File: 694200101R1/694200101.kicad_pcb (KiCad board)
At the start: 2 copper layers, 438.6 x 125.8 mm, 393 parts, among them J1 USB4085-GF-A, J2 Conn_01x05_Male, J3 Conn_01x02_Male, SW1 MX_SW, SW10 MX_SW, SW100 MX_SW, SW101 MX_SW, SW102 MX_SW, SW103 MX_SW, SW104 MX_SW, SW105 MX_SW, SW106 MX_SW, SW107 MX_SW, SW11 MX_SW, SW12 MX_SW, SW13 MX_SW, SW14 MX_SW, SW15 MX_SW, SW16 MX_SW, SW17 MX_SW, SW18 MX_SW, SW19 MX_SW, SW2 MX_SW, SW20 MX_SW, SW21 MX_SW, SW22 MX_SW, SW23 MX_SW, SW24 MX_SW, SW25 MX_SW, SW26 MX_SW, SW27 MX_SW, SW28 MX_SW, SW29 MX_SW, SW3 MX_SW, SW30 MX_SW, SW31 MX_SW, SW32 MX_SW, SW33 MX_SW, SW34 MX_SW, SW35 MX_SW, SW36 MX_SW, SW37 MX_SW, SW38 MX_SW, SW39 MX_SW, SW4 MX_SW, SW40 MX_SW, SW41 MX_SW, SW42 MX_SW, SW43 MX_SW, SW44 MX_SW, SW45 MX_SW, SW46 MX_SW, SW47 MX_SW, SW48 MX_SW, SW49 MX_SW, SW5 MX_SW, SW50 MX_SW, SW51 MX_SW, SW52 MX_SW, SW53 MX_SW, SW54 MX_SW, SW55 MX_SW, SW56 MX_SW, SW57 MX_SW, SW58 MX_SW, SW59 MX_SW, SW6 MX_SW, SW60 MX_SW, SW61 MX_SW, SW62 MX_SW, SW63 MX_SW, SW64 MX_SW, SW65 MX_SW, SW66 MX_SW, SW67 MX_SW, SW68 MX_SW, SW69 MX_SW, SW7 MX_SW, SW70 MX_SW, SW71 MX_SW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

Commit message: Updated PCB Footprints
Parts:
- CR1: value SMAJ9.0CA -> SMASeries_LTF
- F1: value 1210L150THWR -> 1210LSeries_LTF
- U1: value AP2114HA-3.3TRG1 -> SOT-223_DIO
- U5, U6: value IS31FL3733B-QFLS4-TR -> QFN-48_ISI

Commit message: row 6 row traces
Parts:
- CR1: value SMASeries_LTF -> SMAJ9.0CA
- F1: value 1210LSeries_LTF -> 1210L150THWR
- U1: value SOT-223_DIO -> AP2114HA-3.3TRG1
- U5, U6: value QFN-48_ISI -> IS31FL3733B-QFLS4-TR
- moved D96 0.35 mm to (389.9, 46.5)
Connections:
- SW106 pad 1: Net-(D107-Pad2) -> COL_22
- SW106 pad 2: COL_22 -> Net-(D107-Pad2)
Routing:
- net ROW_6: track 0.00 -> 414.6 mm
- net Net-(D94-Pad2): track 0.00 -> 6.35 mm
- net Net-(D99-Pad2): track 0.00 -> 5.18 mm
- net Net-(D19-Pad2): track 0.00 -> 4.81 mm
- net Net-(D78-Pad2): track 0.00 -> 4.80 mm
- net Net-(D68-Pad2): track 0.00 -> 4.71 mm
- net Net-(D93-Pad2): track 0.00 -> 4.67 mm
- net Net-(D54-Pad2): track 0.00 -> 4.58 mm
- net Net-(D67-Pad2): track 0.00 -> 4.57 mm
- net Net-(D5-Pad2): track 0.00 -> 4.54 mm
- net Net-(D108-Pad2): track 0.00 -> 4.38 mm
- net Net-(D8-Pad2): track 0.00 -> 4.37 mm
- net Net-(D70-Pad2): track 0.00 -> 4.31 mm
- net Net-(D37-Pad2): track 0.00 -> 4.24 mm
- net Net-(D73-Pad2): track 0.00 -> 4.22 mm
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
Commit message: Added Mounting Holes and alignment slots
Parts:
- added H1: PCB Mounting Hole, MountingHole:MountingHole_3.5mm, F.Cu at (395.0, 130.8)
- added H2: PCB Common Earth, MountingHole:MountingHole_3.5mm_Pad_TopBottom, F.Cu at (209.6, -6.35)
- added H3: PCB Mounting Hole, MountingHole:MountingHole_3.5mm, F.Cu at (195.6, 134.6)
- added H4: PCB Mounting Hole, MountingHole:MountingHole_3.5mm, F.Cu at (27.9, 132.1)
- added H5: PCB Mounting Hole, MountingHole:MountingHole_3.5mm, F.Cu at (416.6, -5.08)
- added H6: PCB Mounting Hole, MountingHole:MountingHole_3.5mm, F.Cu at (33.0, -6.35)
- added H7: Mounting Slot, keyboard_parts:MountingHole_M2_edge, F.Cu at (436.9, 85.1)
- added H8: Mounting Slot, keyboard_parts:MountingHole_M2_edge, F.Cu at (1.27, 83.8)

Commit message: switch row 3
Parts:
- moved H2 222.9 mm to (432.1, 6.35)
- moved H1 38.8 mm to (432.1, 119.4)
- moved H6 29.5 mm to (6.35, 6.35)
- moved H4 25.0 mm to (6.35, 119.4)
- moved H5 5.48 mm to (411.2, -6.35)
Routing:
- net ROW_5: track 0.00 -> 392.4 mm
- net ROW_4: track 0.00 -> 300.9 mm
- net ROW_3: track 0.00 -> 292.9 mm
- net Net-(D69-Pad2): track 0.00 -> 3.82 mm

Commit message: side slots and switch row 2
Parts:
- moved H2 138.8 mm to (293.2, 6.35)
- moved H8 1.42 mm to (1.91, 85.1)
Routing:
- net ROW_2: track 0.00 -> 414.8 mm, vias 0 -> 2
- net ROW_3: track 292.9 -> 399.3 mm
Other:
- rule trace_min: 0.2 -> 0.2032
- rule via_min_drill: 0.3 -> 0.2032
- rule via_min_size: 0.4 -> 0.3048
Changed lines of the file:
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@@
     (thickness 1.6)
     (drawings 2085)
-    (tracks 790)
+    (tracks 817)
     (zones 0)
     (modules 401)
@@
     (user_trace_width 1.016)
     (user_trace_width 2.032)
+    (user_trace_width 2.54)
     (trace_clearance 0.0254)
     (zone_clearance 0.127)
     (zone_45_only yes)
-    (trace_min 0.2)
+    (trace_min 0.2032)
     (via_size 0.5588)
     (via_drill 0.3048)
-    (via_min_size 0.4)
-    (via_min_drill 0.3)
+    (via_min_size 0.3048)
+    (via_min_drill 0.2032)
     (user_via 0.381 0.2032)
     (user_via 0.508 0.254)
@@
     (uvia_dia 0.3)
     (uvia_drill 0.1)
+    (diff_pair_width 0.2032)
+    (diff_pair_gap 0.25)
     (add_net +3V3)
     (add_net +5V)
@@
   )
   (module keyboard_parts:MountingHole_M2_edge (layer F.Cu)
-    (at 1.27 83.82)
+    (at 1.905 85.09)
     (descr "Mounting Hole 4mm, no annular")
     (tags "mounting hole 4mm no annular")
@@
   )
   (module MountingHole:MountingHole_3.5mm_Pad_TopBottom (layer F.Cu)
-    (at 432.054 6.35)
+    (at 293.243 6.35)
     (descr "Mounting Hole 3.5mm")
     (tags "mounting hole 3.5mm")
@@
   (segment (start 18.335 44.385) (end 18.5 44.55) (width 0.254) (layer B.Cu) (net 7))
   (segment (start 18.335 40.64) (end 18.335 44.385) (width 0.254) (layer B.Cu) (net 7))
+  (segment (start 18.5 48.449999) (end 94.169999 48.449999) (width 0.254) (layer B.Cu) (net 8))
+  (segment (start 94.5 48.449999) (end 170.75 48.449999) (width 0.254) (layer B.Cu) (net 8))
+  (segment (start 170.75 48.449999) (end 208.75 48.449999) (width 0.254) (layer B.Cu) (net 8))
+  (segment (start 208.75 48.449999) (end 247.0375 48.449999) (width 0.254) (layer B.Cu) (net 8))
+  (segment (start 247.0375 48.449999) (end 253.046999 48.449999) (width 0.254) (layer B.Cu) (net 8))
+  (segment (start 253.046999 48.449999) (end 254.381 49.784) (width 0.254) (layer B.Cu) (net 8))
+  (segment (start 304.864001 48.449999) (end 308.75 48.449999) (width 0.254) (layer B.Cu) (net 8))
+  (segment (start 303.53 49.784) (end 304.864001 48.449999) (width 0.254) (layer B.Cu) (net 8))
+  (segment (start 275.75 49.624) (end 275.59 49.784) (width 0.254) (layer B.Cu) (net 8))
+  (segment (start 275.75 48.449999) (end 275.75 49.624) (width 0.254) (layer B.Cu) (net 8))
+  (segment (start 275.59 49.784) (end 303.53 49.784) (width 0.254) (layer B.Cu) (net 8))
+  (segment (start 254.381 49.784) (end 275.59 49.784) (width 0.254) (layer B.Cu) (net 8))
+  (segment (start 308.75 48.449999) (end 328 48.449999) (width 0.254) (layer B.Cu) (net 8))
+  (segment (start 347.0375 48.449999) (end 349.949001 48.449999) (width 0.254) (layer B.Cu) (net 8))
+  (segment (start 428.25 48.449999) (end 408.9625 48.449999) (width 0.254) (layer B.Cu) (net 8))
+  (segment (start 328 48.449999) (end 333.437999 48.449999) (width 0.254) (layer B.Cu) (net 8))
+  (segment (start 333.437999 48.449999) (end 339.406999 48.449999) (width 0.254) (layer B.Cu) (net 8))
+  (segment (start 339.406999 48.449999) (end 339.406999 48.449999) (width 0.254) (layer B.Cu) (net 8))
+  (via (at 339.406999 48.449999) (size 0.508) (drill 0.254) (layers F.Cu B.Cu) (net 8))
+  (segment (start 349.949001 48.449999) (end 408.9625 48.449999) (width 0.254) (layer B.Cu) (net 8))
+  (via (at 349.949001 48.449999) (size 0.508) (drill 0.254) (layers F.Cu B.Cu) (net 8))
+  (segment (start 339.406999 48.449999) (end 349.949001 48.449999) (width 0.254) (layer F.Cu) (net 8))
   (segment (start 23.0975 63.1475) (end 23.25 63.3) (width 0.254) (layer B.Cu) (net 9))
   (segment (start 23.0975 59.69) (end 23.0975 63.1475) (width 0.254) (layer B.Cu) (net 9))
@@
   (segment (start 263.271 65.405) (end 286.385 65.405) (width 0.254) (layer B.Cu) (net 10))
   (segment (start 252.476 65.405) (end 263.271 65.405) (width 0.254) (layer B.Cu) (net 10))
+  (segment (start 309 67.199999) (end 328 67.199999) (width 0.254) (layer B.Cu) (net 10))
+  (segment (start 328 67.199999) (end 370.75 67.199999) (width 0.254) (layer B.Cu) (net 10))
+  (segment (start 370.75 67.199999) (end 408.75 67.199999) (width 0.254) (layer B.Cu) (net 10))
+  (segment (start 411.75 67.199999) (end 414.300001 69.75) (width 0.254) (layer B.Cu) (net 10))
+  (segment (start 408.75 67.199999) (end 411.75 67.199999) (width 0.254) (layer B.Cu) (net 10))
   (segment (start 25.47875 82.02875) (end 25.5 82.05) (width 0.254) (layer B.Cu) (net 11))
   (segment (start 25.47875 78.74) (end 25.47875 82.02875) (width 0.254) (layer B.Cu) (net 11))

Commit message: 6mh placed
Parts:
- moved H1 307.5 mm to (153.3, -10.4)
- moved H4 206.1 mm to (166.8, -10.0)
- moved H3 31.7 mm to (167.8, 119.5)
- moved H6 31.4 mm to (33.1, 22.7)
- moved H5 29.3 mm to (414.9, 22.7)
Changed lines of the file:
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@@
   )
   (module MountingHole:MountingHole_3.5mm (layer F.Cu)
-    (at 6.35 6.35)
+    (at 33.147 22.733)
     (descr "Mounting Hole 3.5mm, no annular")
     (tags "mounting hole 3.5mm no annular")
@@
   )
   (module MountingHole:MountingHole_3.5mm (layer F.Cu)
-    (at 411.226 -6.35)
+    (at 414.909 22.733)
     (descr "Mounting Hole 3.5mm, no annular")
     (tags "mounting hole 3.5mm no annular")
@@
   )
   (module MountingHole:MountingHole_3.5mm (layer F.Cu)
-    (at 6.35 119.38)
+    (at 166.751 -10.033)
     (descr "Mounting Hole 3.5mm, no annular")
     (tags "mounting hole 3.5mm no annular")
@@
   )
   (module MountingHole:MountingHole_3.5mm (layer F.Cu)
-    (at 195.58 134.62)
+    (at 167.767 119.507)
     (descr "Mounting Hole 3.5mm, no annular")
     (tags "mounting hole 3.5mm no annular")
@@
   )
   (module MountingHole:MountingHole_3.5mm (layer F.Cu)
-    (at 432.054 119.38)
+    (at 153.289 -10.414)
     (descr "Mounting Hole 3.5mm, no annular")
     (tags "mounting hole 3.5mm no annular")

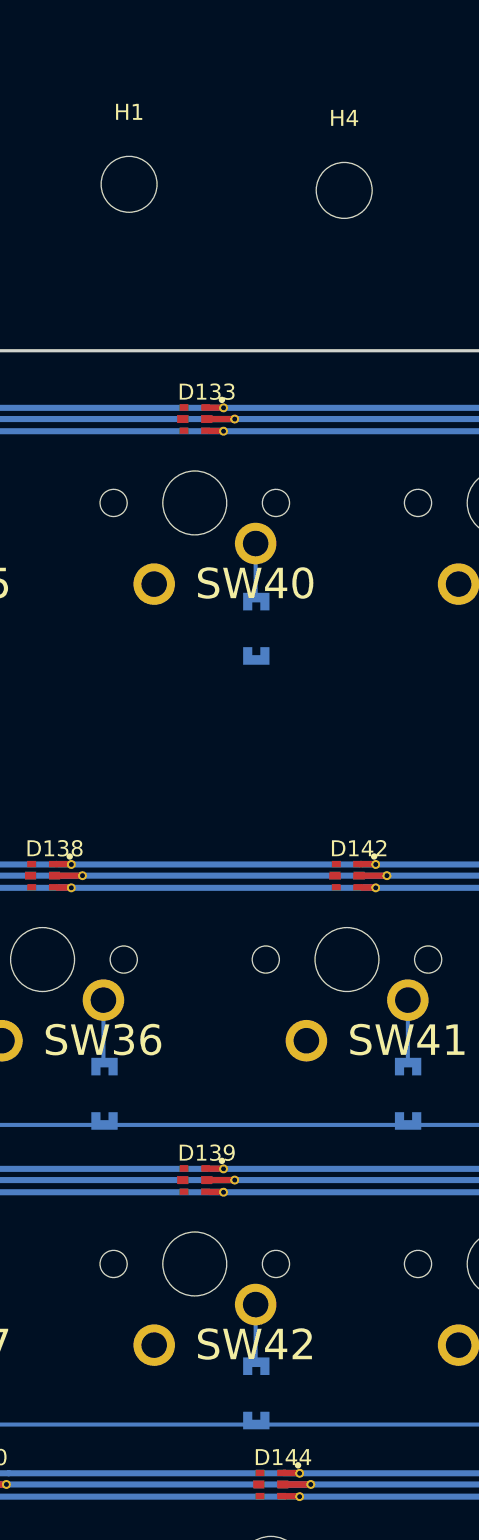
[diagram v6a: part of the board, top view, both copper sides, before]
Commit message: h1 to middle
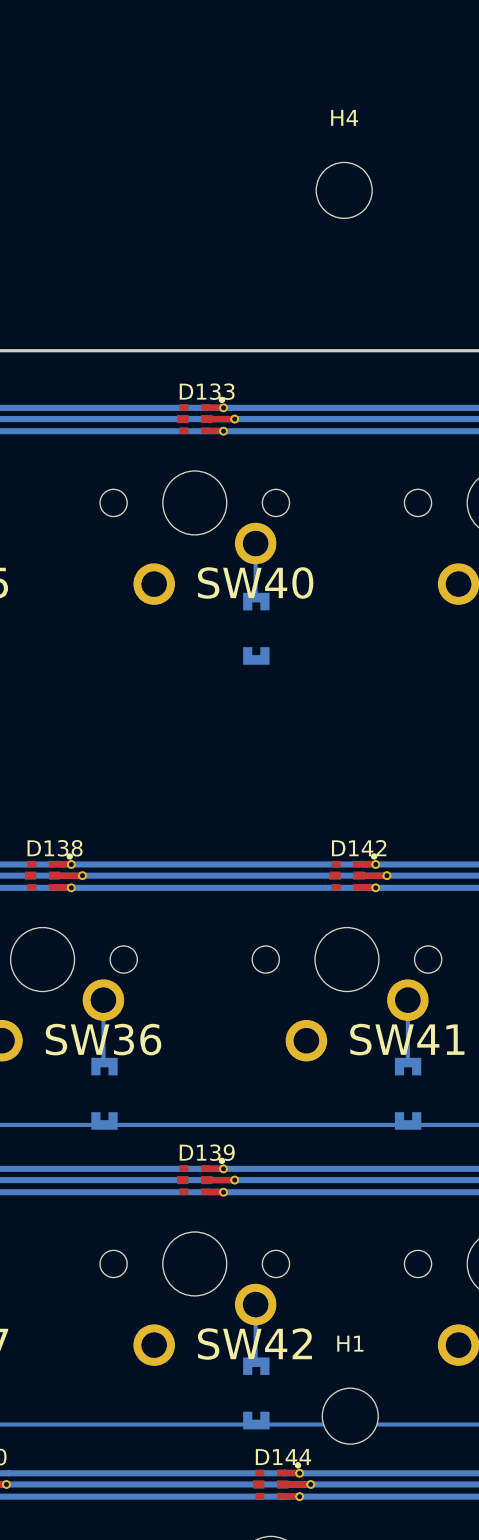
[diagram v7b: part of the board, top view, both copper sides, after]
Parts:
- moved H1 78.3 mm to (167.1, 66.7)
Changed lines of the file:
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@@
   )
   (module MountingHole:MountingHole_3.5mm (layer F.Cu)
-    (at 153.289 -10.414)
+    (at 167.132 66.675)
     (descr "Mounting Hole 3.5mm, no annular")
     (tags "mounting hole 3.5mm no annular")

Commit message: begun mcu
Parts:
- R10, R9: moved to B.Cu
- moved J2 149.1 mm to (309.8, 25.4)
- moved J3 149.1 mm to (305.5, 26.4)
- moved C12 134.3 mm to (331.5, -36.8)
- moved C13 134.3 mm to (330.6, -25.4)
- moved C14 134.3 mm to (332.1, -25.4)
- moved C16 134.3 mm to (337.1, -29.7)
- moved C17 134.3 mm to (340.4, -29.1)
- moved R15 134.3 mm to (325.2, -33.8)
- moved R16 134.3 mm to (323.7, -34.4)
- moved R17 134.3 mm to (335.8, -35.9)
- moved U5 134.3 mm to (330.1, -31.2)
- moved C11 134.3 mm to (333.1, -36.8)
- moved C15 134.3 mm to (335.4, -29.8)
- moved U6 132.0 mm to (383.1, -30.6), turned to 0 degrees
- moved R10 52.7 mm to (346.7, 21.5), turned to 270 degrees
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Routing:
- net ROW_0: track 0.00 -> 301.6 mm
- net USB_D+: track 15.5 -> 24.4 mm
- net USB_D-: track 16.2 -> 24.4 mm
- net Net-(ENC1-PadB1): track 0.00 -> 5.72 mm
- net Net-(ENC1-PadA1): track 0.00 -> 2.13 mm
- net ENCODER_A: track 0.00 -> 1.84 mm
- net ENCODER_B: track 0.00 -> 1.71 mm
- net +5V: track 17.8 -> 16.6 mm
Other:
- net class Default: clearance 0.0254 -> 0.0762
- rule trace_clearance: 0.0254 -> 0.0762
